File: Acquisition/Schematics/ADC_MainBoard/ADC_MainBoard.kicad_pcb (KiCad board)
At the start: 2 copper layers, 44.4 x 33 mm, 49 parts, among them J1 Conn_02x06_Counter_Clockwise, J13 Conn_01x02_Pin, J14 Pad, J15 Pad, J16 Pad, J17 Pad, J2 Pad, J3 Pad, J5 2004850720, J6 Conn_02x06_Counter_Clockwise, J7 Pad, J8 Pad, J9 Pad, U1 MCP1525-TT, U3 OPA333xxDBV, U5 LP5907MFX-2.8, U6 LP5907MFX-1.2, U7 LD1117S33TR_SOT223

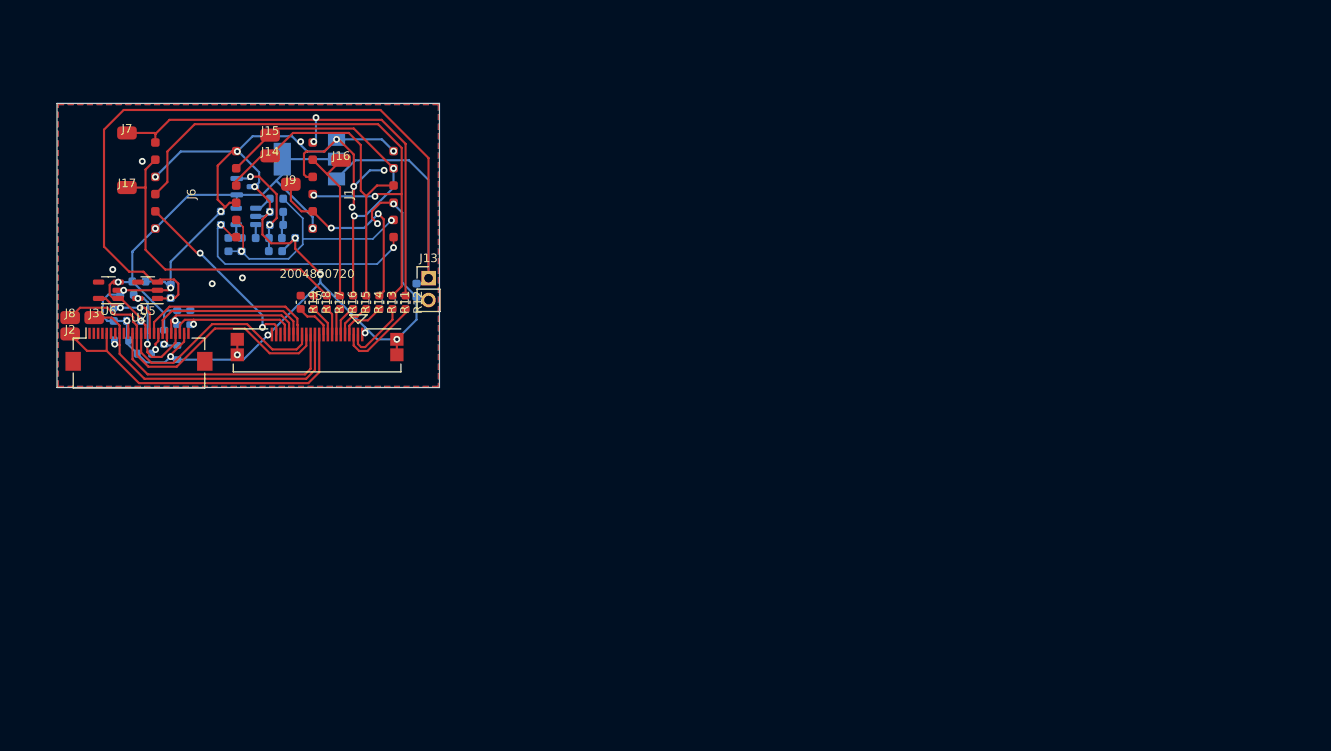
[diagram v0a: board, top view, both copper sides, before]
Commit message: Schematics - FPGA board seems done
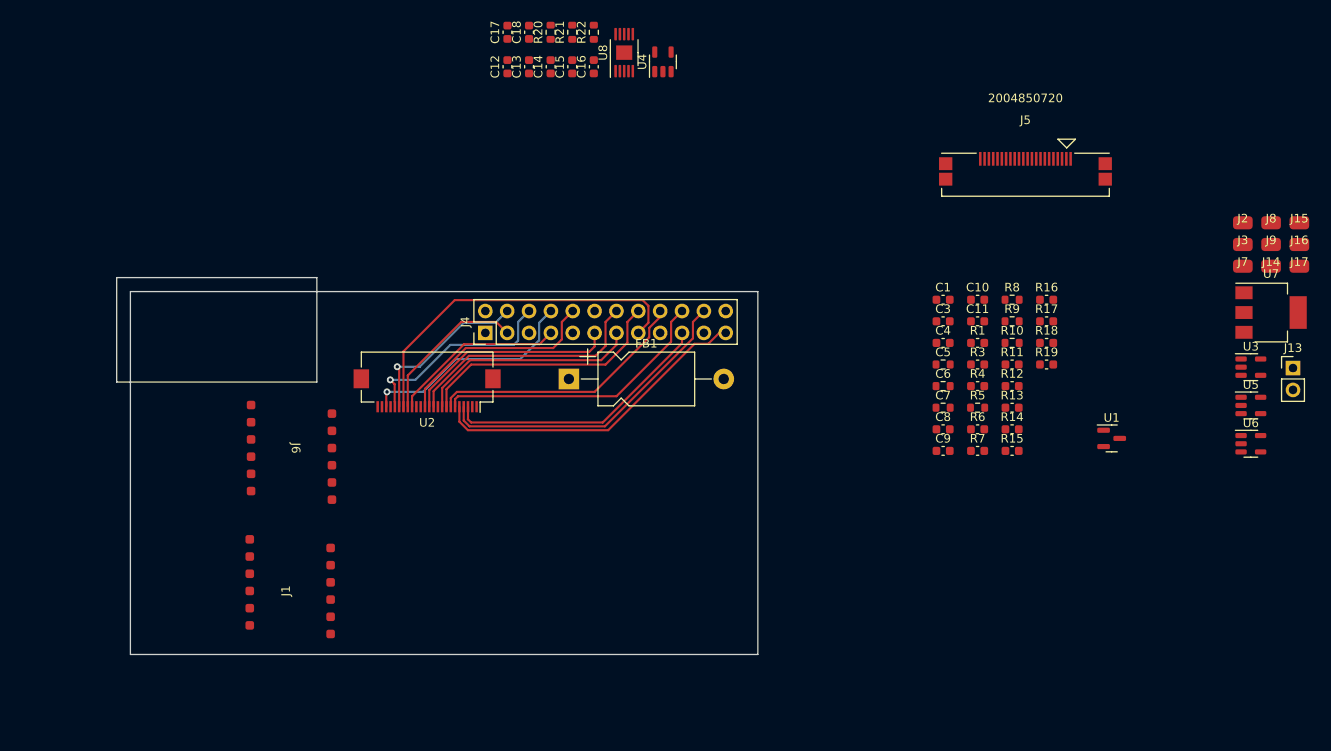
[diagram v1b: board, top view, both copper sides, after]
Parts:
- removed C2: 100n, Capacitor_SMD:C_0603_1608Metric
- removed R2: 1K, Capacitor_SMD:C_0603_1608Metric
- added C12: 100n, Capacitor_SMD:C_0603_1608Metric, F.Cu at (106.3, 32.2)
- added C13: 100n, Capacitor_SMD:C_0603_1608Metric, F.Cu at (108.8, 32.2)
- added C14: 100n, Capacitor_SMD:C_0603_1608Metric, F.Cu at (111.3, 32.2)
- added C15: 100n, Capacitor_SMD:C_0603_1608Metric, F.Cu at (113.9, 32.2)
- added C16: 4.7u, Capacitor_SMD:C_0603_1608Metric, F.Cu at (116.4, 32.2)
- added C17: 4.7u, Capacitor_SMD:C_0603_1608Metric, F.Cu at (106.3, 28.2)
- added C18: 470n, Capacitor_SMD:C_0603_1608Metric, F.Cu at (108.8, 28.2)
- added FB1: FerriteBead, Capacitor_THT:CP_Axial_L11.0mm_D6.0mm_P18.00mm_Horizontal, F.Cu at (113.5, 68.5)
- added J4: Conn_02x12_Odd_Even, Connector_PinHeader_2.54mm:PinHeader_2x12_P2.54mm_Vertical, F.Cu at (103.8, 63.1)
- added R20: 0, Resistor_SMD:R_0603_1608Metric, F.Cu at (111.3, 28.2)
- added R21: 0, Resistor_SMD:R_0603_1608Metric, F.Cu at (113.9, 28.2)
- added R22: 33.2k, Resistor_SMD:R_0603_1608Metric, F.Cu at (116.4, 28.2)
- added U4: TPS7A2033, Package_TO_SOT_SMD:SOT-23-5, F.Cu at (124.4, 31.6)
- added U8: LT3042xMSE, Package_SO:MSOP-10-1EP_3x3mm_P0.5mm_EP1.68x1.88mm, F.Cu at (119.9, 30.5)
- C1, C10, C11, C3, C4, C5, C6, C7, C8, C9, R10, R3, R4, R5, R6, R7, R8, R9, U1, U3, U7: moved to F.Cu
- R1: value 1K -> 0; moved to F.Cu
- moved J8 140.0 mm to (195.1, 50.3)
- moved J2 136.9 mm to (191.8, 50.3)
- moved J17 136.6 mm to (198.4, 55.4)
- moved U6 134.0 mm to (192.7, 76.0), turned to 0 degrees
- moved J3 133.8 mm to (191.8, 52.8)
- moved J7 130.6 mm to (191.8, 55.4)
- moved U5 128.9 mm to (192.7, 71.6), turned to 0 degrees
- moved J15 120.1 mm to (198.4, 50.3)
- moved U3 118.1 mm to (192.7, 67.1), turned to 0 degrees
- moved J14 117.1 mm to (195.1, 55.4)
- moved J9 114.2 mm to (195.1, 52.8)
- moved U7 113.2 mm to (195.1, 60.8), turned to 0 degrees
- moved J16 111.8 mm to (198.4, 52.8)
- moved U1 104.9 mm to (176.6, 75.4)
- moved R8 101.0 mm to (165.0, 59.3), turned to 0 degrees
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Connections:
- net Net-(U2-PWDN) renamed /CamPWDN
- C1 pad 2: Earth -> GND
- C5 pad 1: /PCLK -> /CamPCLK
- C7 pad 2: Earth -> GND
- C8 pad 1: +5V -> +5VA
- J1 pad 1: /REFIN- -> /AVdd
- J1 pad 10: /nCS -> /nIRQ
- J1 pad 11: /nIRQ -> Earth
- J1 pad 12: +3.3V -> GND
- J1 pad 6: Earth -> +3.3V
- J1 pad 9: Earth -> /nCS
- J6 pad 1: /REFIN- -> /AVdd
- J6 pad 11: /nIRQ___2 -> unconnected-(J6-Pin_11-Pad11)
- J6 pad 3: Earth -> GND
- J6 pad 6: Earth -> GND
- J6 pad 9: Earth -> GND
- R1 pad 1: Earth -> Net-(U1-Vout)
- R1 pad 2: Net-(C2-Pad2) -> /REFIN+
- R4 pad 1: /REFIN- -> GND
- U1 pad 1: +3.3V -> +3.3VA
- U1 pad 3: Earth -> GND
- U2 pad 23: Earth -> GND
- U2 pad 8: /PCLK -> /CamPCLK
- U3 pad 2: Earth -> GND
- U3 pad 5: +3.3V -> +3.3VA
- U5 pad 1: +5V -> +5VA
- U5 pad 3: +5V -> +5VA
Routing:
- net Earth: track 195.0 -> 0.00 mm, vias 27 -> 0
- net +5V: track 108.7 -> 0.00 mm, vias 1 -> 0
- net /nCS: track 63.4 -> 0.00 mm, vias 2 -> 0
- net +3.3V: track 62.7 -> 0.00 mm, vias 4 -> 0
- net /MCLK: track 56.0 -> 0.00 mm, vias 2 -> 0
- net /SDI: track 39.6 -> 0.00 mm, vias 2 -> 0
- net /SCK: track 39.2 -> 0.00 mm
- net /CamD1: track 0.00 -> 36.5 mm
- net /SDO2: track 36.4 -> 0.00 mm
- net /PCLK: track 35.7 -> 0.00 mm, vias 1 -> 0
- net /CamD0: track 0.00 -> 32.8 mm
- net /CamD2: track 0.00 -> 31.5 mm
- net /REFIN+: track 31.5 -> 0.00 mm, vias 2 -> 0
- net /CamD4: track 0.00 -> 30.6 mm
- net /CamPCLK: track 0.00 -> 29.9 mm
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- removed copper zone on B.Cu, net Earth
- removed copper zone on F.Cu, net Earth
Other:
- board size 44.4 x 33 mm -> 74.5 x 43.8 mm
- copper layers 2 -> 4

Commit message: Acquisition schematics should be working.
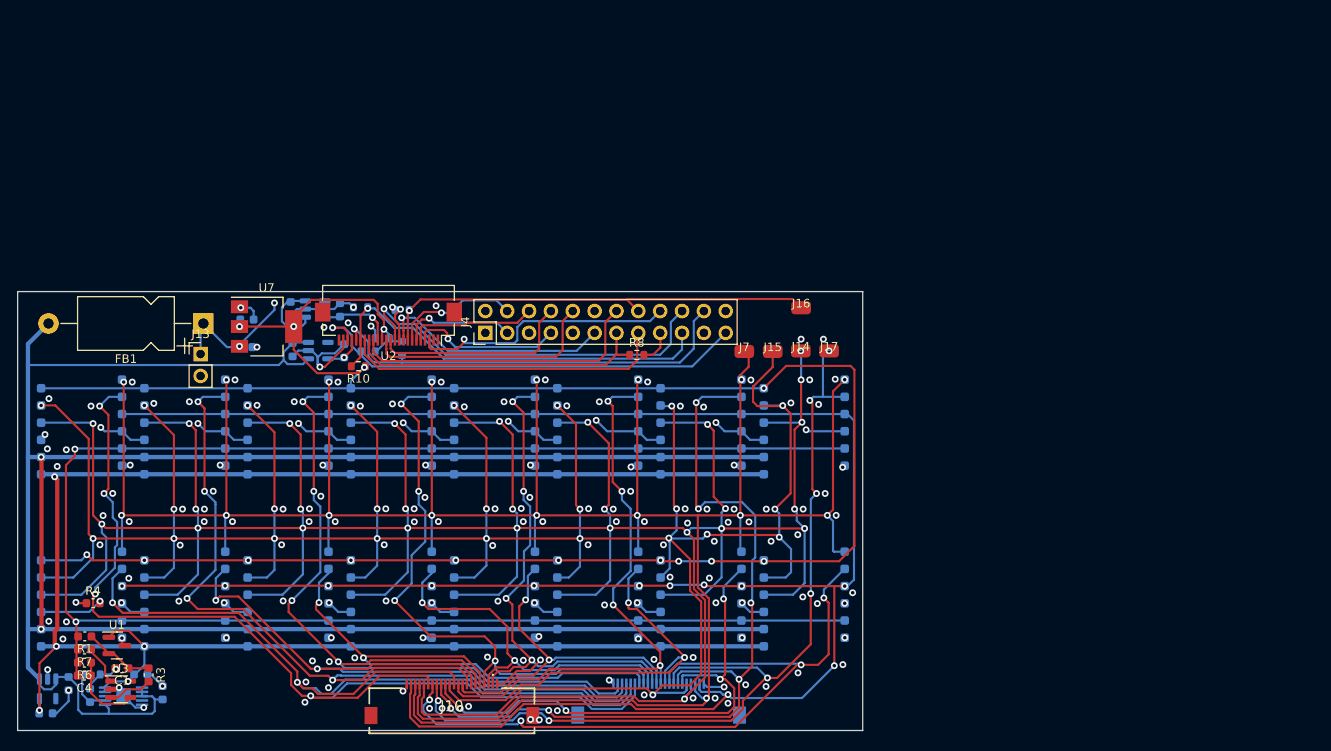
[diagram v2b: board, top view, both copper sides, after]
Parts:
- removed C15: 100n, Capacitor_SMD:C_0603_1608Metric
- removed J2, J3, J8, J9: Pad, CustomLibrary:Pad
- removed J6: Conn_02x06_Counter_Clockwise, CustomLibrary:KYOCERA AVX Base
- removed R11, R12, R13, R14, R15, R16, R17, R18, R19: 10, Capacitor_SMD:C_0603_1608Metric
- removed R20, R21: 0, Resistor_SMD:R_0603_1608Metric
- added J10: 2004850720, CustomLibrary:Molex FFC 20pin sideways, F.Cu at (99.9, 106.8)
- added J11: ADC_Conn, CustomLibrary:KYOCERA AVX Base, B.Cu at (128.8, 94.6)
- added J12: ADC_Conn, CustomLibrary:KYOCERA AVX Base, B.Cu at (116.8, 94.6)
- added J18: ADC_Conn, CustomLibrary:KYOCERA AVX Base, B.Cu at (104.8, 94.6)
- added J19: ADC_Conn, CustomLibrary:KYOCERA AVX Base, B.Cu at (92.8, 94.6)
- added J20: ADC_Conn, CustomLibrary:KYOCERA AVX Base, B.Cu at (80.8, 94.6)
- added J21: ADC_Conn, CustomLibrary:KYOCERA AVX Base, B.Cu at (68.8, 94.6)
- added J22: ADC_Conn, CustomLibrary:KYOCERA AVX Base, B.Cu at (104.8, 74.6)
- added J23: ADC_Conn, CustomLibrary:KYOCERA AVX Base, B.Cu at (92.8, 74.6)
- added J24: ADC_Conn, CustomLibrary:KYOCERA AVX Base, B.Cu at (80.8, 74.6)
- added J25: ADC_Conn, CustomLibrary:KYOCERA AVX Base, B.Cu at (68.8, 74.6)
- added J26: ADC_Conn, CustomLibrary:KYOCERA AVX Base, B.Cu at (56.8, 74.6)
- added J27: ADC_Conn, CustomLibrary:KYOCERA AVX Base, B.Cu at (140.8, 94.6)
- added J28: ADC_Conn, CustomLibrary:KYOCERA AVX Base, B.Cu at (140.8, 74.6)
- added J29: ADC_Conn, CustomLibrary:KYOCERA AVX Base, B.Cu at (128.8, 74.6)
- added J30: ADC_Conn, CustomLibrary:KYOCERA AVX Base, B.Cu at (116.8, 74.6)
- C10, C11, C12, C13, C14, C16, C17, C18, C3, C5, C6, C7, C8, C9, R22, R5, R9, U4, U5, U6, U8: moved to B.Cu
- J1: value Conn_02x06_Counter_Clockwise -> ADC_Conn; moved to B.Cu
- J5: footprint footprints:CON_2004850720 -> CustomLibrary:Molex FFC 20pin sideways; moved to B.Cu
- moved U3 136.6 mm to (61.4, 104.5)
- moved J13 127.0 mm to (70.7, 65.6)
- moved U1 118.1 mm to (60.9, 99.5)
- moved U7 116.8 mm to (78.3, 62.4)
- moved U6 109.9 mm to (84.0, 60.4)
- moved R1 109.2 mm to (57.2, 98.4), turned to 180 degrees
- moved U5 108.6 mm to (84.3, 65.2)
- moved R6 107.3 mm to (57.2, 101.4), turned to 180 degrees
- moved C4 107.0 mm to (57.1, 103.0), turned to 180 degrees
- moved R7 106.3 mm to (57.2, 99.9), turned to 180 degrees
- moved R4 105.9 mm to (58.2, 94.5)
- moved C1 104.6 mm to (61.5, 102.1), turned to 180 degrees
- moved R3 102.9 mm to (64.6, 102.9), turned to -90 degrees
- moved U4 102.1 mm to (52.9, 104.5), turned to -90 degrees
- moved C14 95.3 mm to (52.7, 107.3), turned to 0 degrees
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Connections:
- C7 pad 2: GND -> Earth
- C8 pad 2: Earth -> GND
- C9 pad 2: Earth -> GND
- J1 pad 1: /AVdd -> +3.3VA
- J1 pad 10: /nIRQ -> Earth
- J1 pad 11: Earth -> /REFIN+
- J1 pad 2: /REFIN+ -> +5VA
- J1 pad 8: /SDO1 -> /SDO10
- J16 pad 1: /SDO1 -> /CamPCLK
- J17 pad 1: /SDO2 -> /SDO1D
- J4 pad 11: /CamMCLK -> /CamD5
- J4 pad 13: /CamD5 -> /CamPWDN
- J4 pad 14: /CamD6 -> /CamHSYNC
- J4 pad 18: /CamD4 -> /CamD2
- J4 pad 19: /CamD2 -> /CamRST
- J4 pad 2: /5v -> +5V
- J4 pad 20: /CamD0 -> /CamD6
- J4 pad 22: /CamD1 -> /CamSCK
- J4 pad 23: /CamD3 -> /CamSDA
- J4 pad 3: /CamPWDN -> /CamD0
- J4 pad 4: /CamRST -> /CamD4
- J4 pad 6: /CamSCK -> /CamD3
- J4 pad 7: /CamHSYNC -> /CamD1
- J4 pad 8: /CamSDA -> /CamMCLK
- J5 pad 1: Net-(J5-Pad1) -> /SDO19
- J5 pad 10: /CamD3 -> /SDO13
- J5 pad 11: /PCLK -> /SDO1F
- J5 pad 12: /CamD6 -> /SDO12
- J5 pad 13: /CamMCLK -> /SDO1C
- J5 pad 14: /CamD7 -> /SDO1D
- J5 pad 15: /CamHSYNC -> /SDO1E
- J5 pad 16: /CamVSYNC -> /SDO11
- J5 pad 17: /CamSCK -> /SDI
- J5 pad 18: /CamSDA -> /SCK
- J5 pad 19: /nIRQ___3 -> /MCLK
- J5 pad 2: Net-(J5-Pad2) -> /SDO16
- J5 pad 20: /nIRQ___2 -> /nCS
- J5 pad 3: Net-(J5-Pad3) -> /SDO1A
- J5 pad 4: Net-(J5-Pad4) -> /SDO10
- J5 pad 5: Net-(J5-Pad5) -> /SDO1B
- J5 pad 6: Net-(J5-Pad6) -> /SDO15
- J5 pad 7: Net-(J5-Pad7) -> /SDO18
- J5 pad 8: Net-(J5-Pad8) -> /SDO14
- J5 pad 9: Net-(J5-Pad9) -> /SDO17
- U5 pad 2: Earth -> GND
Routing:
- net /SCK: track 0.00 -> 398.6 mm, vias 0 -> 27
- net /SDI: track 0.00 -> 347.9 mm, vias 0 -> 25
- net /MCLK: track 0.00 -> 313.5 mm, vias 0 -> 17
- net +5VA: track 0.00 -> 296.5 mm, vias 0 -> 2
- net +3.3V: track 0.00 -> 265.6 mm, vias 0 -> 15
- net /nCS: track 0.00 -> 260.8 mm, vias 0 -> 12
- net +3.3VA: track 0.00 -> 212.1 mm, vias 0 -> 5
- net /REFIN+: track 0.00 -> 206.2 mm, vias 0 -> 2
- net Earth: track 0.00 -> 167.8 mm, vias 0 -> 142
- net /SDO1B: track 0.00 -> 116.8 mm, vias 0 -> 4
- net /SDO1D: track 0.00 -> 104.0 mm, vias 0 -> 7
- net /SDO1A: track 0.00 -> 104.0 mm, vias 0 -> 4
- net /SDO1E: track 0.00 -> 95.8 mm, vias 0 -> 6
- net /SDO10: track 0.00 -> 94.5 mm, vias 0 -> 2
- net /SDO19: track 0.00 -> 91.3 mm, vias 0 -> 4
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- added copper zone on In1.Cu, net Earth
- added copper zone on In2.Cu, net Earth
- added copper zone on In1.Cu, net GND
- added copper zone on In2.Cu, net GND
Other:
- board size 74.5 x 43.8 mm -> 98.2 x 51 mm

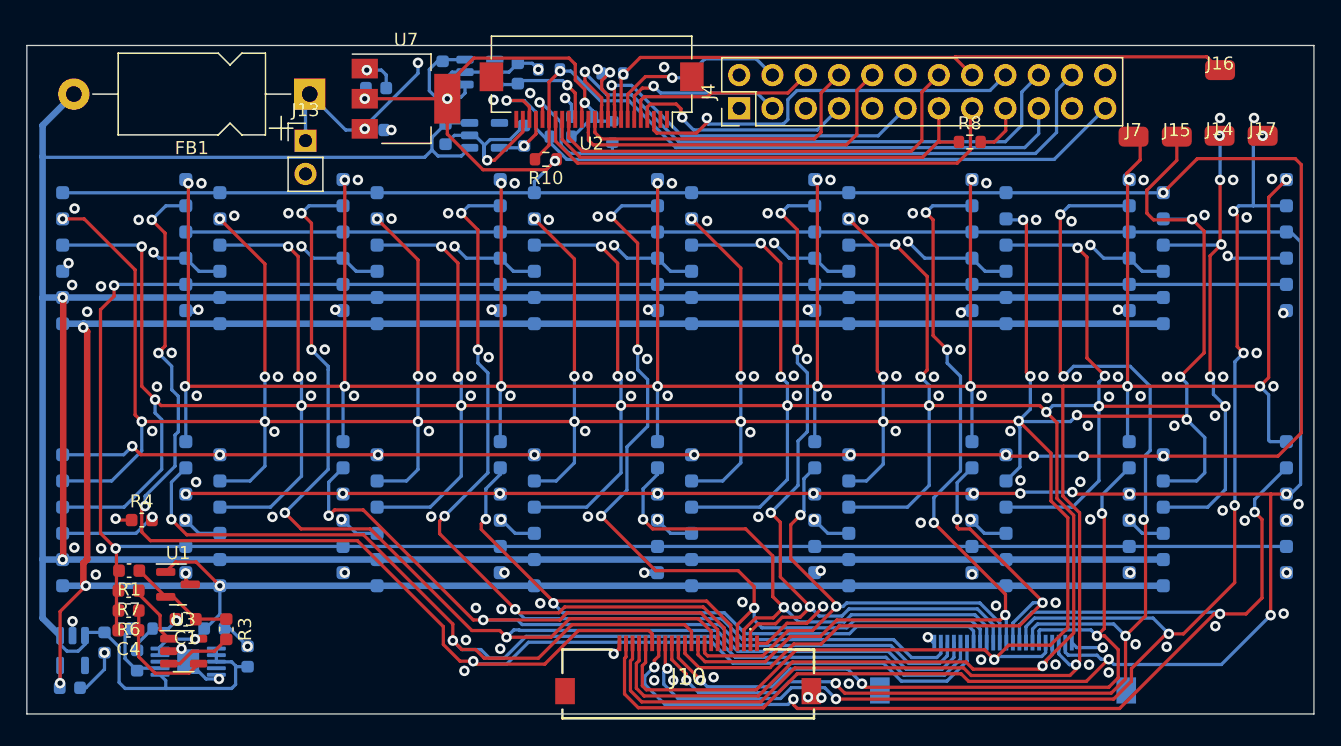
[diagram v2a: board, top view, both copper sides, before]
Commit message: PCBs production ready
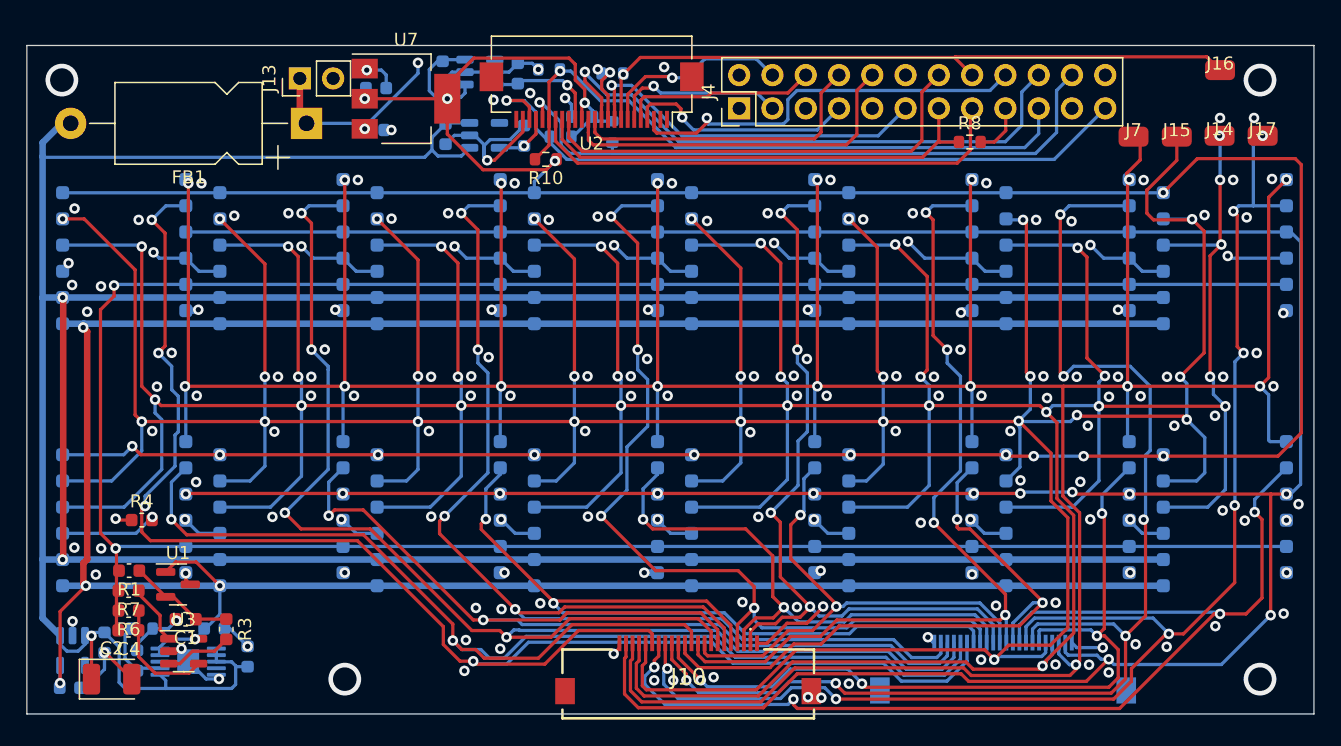
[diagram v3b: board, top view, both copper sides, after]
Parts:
- added C2: 100n, Capacitor_Tantalum_SMD:CP_EIA-3528-21_Kemet-B, F.Cu at (55.9, 106.7)
- moved J13 4.77 mm to (70.2, 60.8), turned to 90 degrees
- moved FB1 2.25 mm to (70.7, 64.3)
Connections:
- net /SDO17 renamed /SDO05
- net /SDO18 renamed /SDO04
- net /SDO19 renamed /SDO03
- net /SDO1A renamed /SDO02
- net /SDO1B renamed /SDO01
- net /SDO1D renamed /SDO08
- net /SDO1E renamed /SDO07
- net /SDO1F renamed /SDO06
- J1 pad 8: /SDO10 -> /SDO09
- J10 pad 10: /SDO10 -> /SDO09
- J10 pad 11: /SDO12 -> /SDO14
- J10 pad 12: /SDO11 -> /SDO15
- J10 pad 15: /SDO1C -> /SDO16
- J10 pad 2: /SDO14 -> /SDO12
- J10 pad 4: /SDO15 -> /SDO11
- J10 pad 6: /SDO16 -> /SDO10
- J11 pad 8: /SDO11 -> /SDO15
- J12 pad 8: /SDO12 -> /SDO14
- J19 pad 8: /SDO14 -> /SDO12
- J20 pad 8: /SDO15 -> /SDO11
- J21 pad 8: /SDO16 -> /SDO10
- J27 pad 8: /SDO1C -> /SDO16
- J5 pad 12: /SDO12 -> /SDO14
- J5 pad 13: /SDO1C -> /SDO16
- J5 pad 16: /SDO11 -> /SDO15
- J5 pad 2: /SDO16 -> /SDO10
- J5 pad 4: /SDO10 -> /SDO09
- J5 pad 6: /SDO15 -> /SDO11
- J5 pad 8: /SDO14 -> /SDO12
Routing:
- net /SDO09: track 0.00 -> 94.5 mm, vias 0 -> 2
- net /SDO1C: track 83.8 -> 0.00 mm, vias 4 -> 0
- net /SDO10: track 94.5 -> 77.3 mm
- net /SDO14: track 42.3 -> 48.9 mm
- net /SDO12: track 48.9 -> 42.3 mm
- net /SDO16: track 77.3 -> 83.8 mm, vias 2 -> 4
- net GND: track 53.6 -> 56.5 mm
- net /SDO15: track 63.3 -> 60.9 mm, vias 2 -> 4
- net /SDO11: track 60.9 -> 63.3 mm, vias 4 -> 2
- net +5VA: track 296.5 -> 298.4 mm, vias 2 -> 3
- net +5V: track 41.8 -> 41.1 mm
- net (no net): vias 0 -> 4
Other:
- board text added: "+5v"
- board text added: "01"
- board text added: "02"
- board text added: "03"
- board text added: "04"
- board text added: "05"
- board text added: "06"
- board text added: "07"
- board text added: "08"
- board text added: "09"
- board text added: "10"
- board text added: "11"
- board text added: "12"
- board text added: "13"
- board text added: "14"
- board text added: "15"
- board text added: "16"
- board text added: "BFM"
- board text added: "MCLK"
- board text added: "PCLK"
- board text added: "SCK"
- board text added: "SDI"
- board text added: "SDO"
